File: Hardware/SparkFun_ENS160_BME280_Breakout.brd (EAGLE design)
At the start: 25.4 x 25.4 mm, 65 parts, among them J1 Qwiic Right Angle, J3 Qwiic Right Angle, J4 PTH, U1 AP2127K-1.8V, U2 ENS-160, U3 BME280

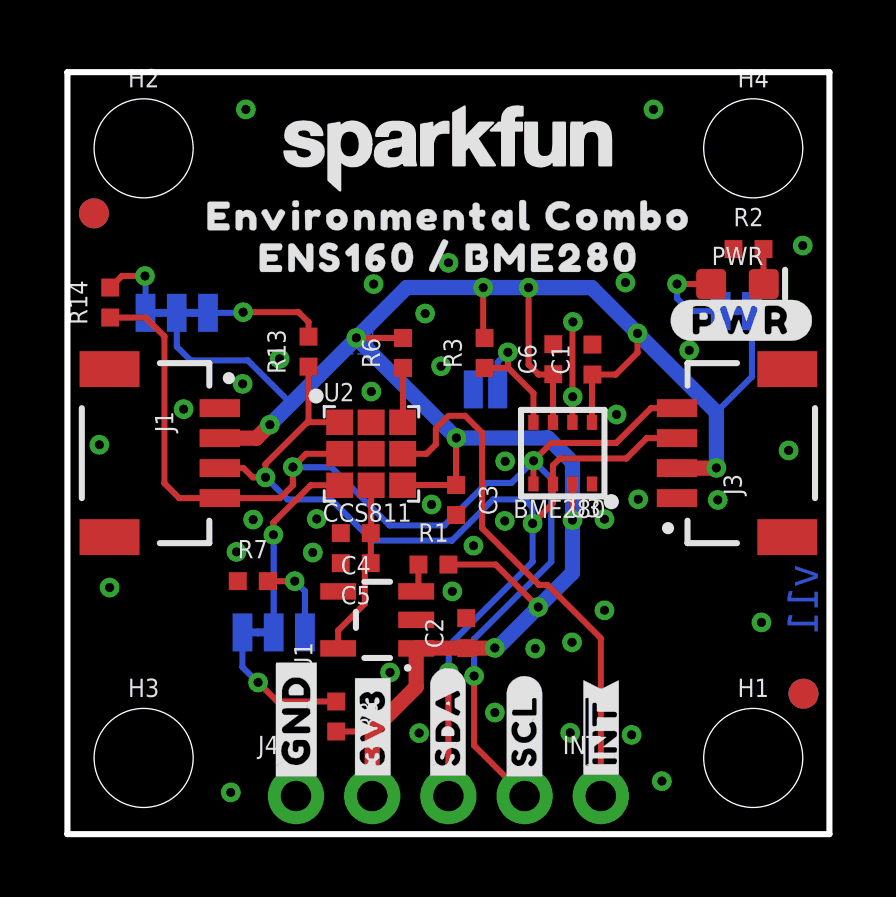
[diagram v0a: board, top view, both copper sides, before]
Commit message: group review changes - qwiic logos, via nudging
-added Qwiic logos to top silk
-nudged some filter caps near the ENS160 to allow even better GND flow
-removed old "ADDR" silk object on bottom silk.
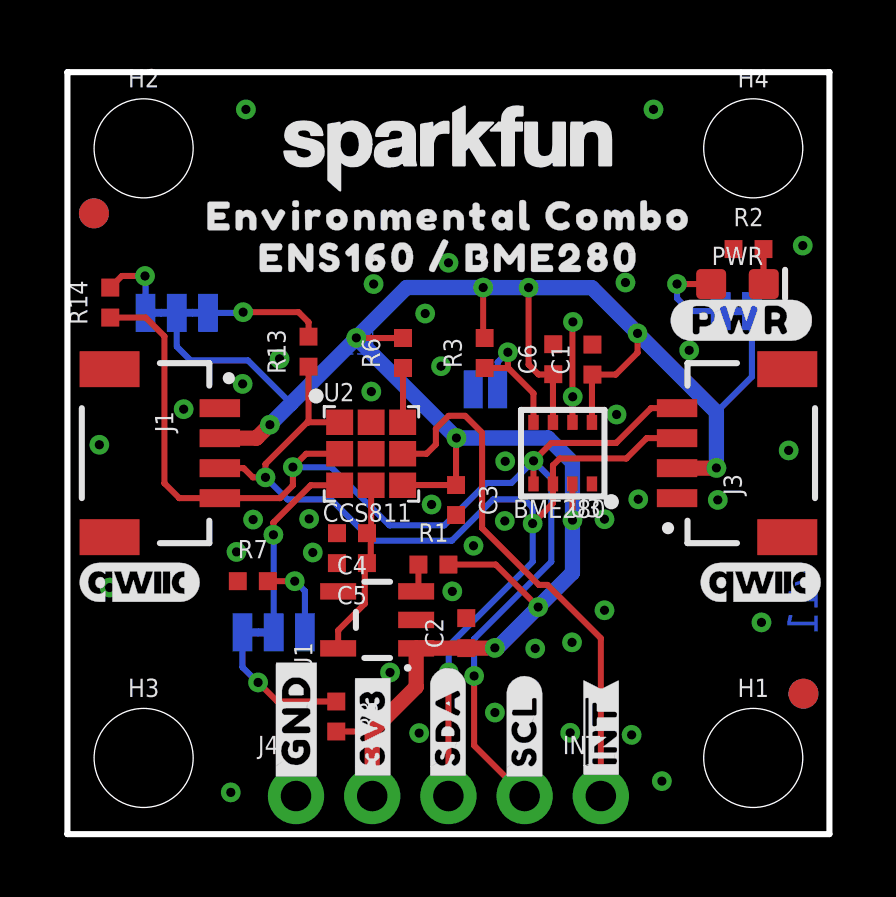
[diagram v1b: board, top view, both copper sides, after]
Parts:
- added U$20, U$21: (no value), SparkFun-Aesthetics:QWIIC_4MM
- moved U$17 0.38 mm to (17.9, 11.7)
- moved U$16 0.13 mm to (17.0, 13.1)
- moved C4 0.13 mm to (9.49, 10.0)
- moved C5 0.13 mm to (9.48, 9.03)
- moved U$61 0.13 mm to (9.84, 13.1)
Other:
- board text removed: "ADR1"
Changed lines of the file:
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@@
 <setting verticaltext="up"/>
 </settings>
-<grid distance="0.05" unitdist="inch" unit="inch" style="lines" multiple="1" display="yes" altdistance="0.0001" altunitdist="inch" altunit="inch"/>
+<grid distance="0.05" unitdist="inch" unit="inch" style="lines" multiple="1" display="yes" altdistance="0.005" altunitdist="inch" altunit="inch"/>
 <layers>
 <layer number="1" name="Top" color="4" fill="1" visible="yes" active="yes"/>
@@
 <wire x1="25.4" y1="0" x2="0" y2="0" width="0.2032" layer="20"/>
 <text x="24.50591875" y="7.8105" size="1.016" layer="16" ratio="20" rot="SMR270" align="center">v11</text>
-<text x="4.572" y="12.827" size="0.889" layer="22" font="vector" ratio="15" rot="MR90" align="center">ADR1</text>
 <text x="16.51" y="-21.59" size="1.778" layer="51">Nathan Seidle</text>
 <text x="8.509" y="10.414" size="0.6096" layer="25">CCS811</text>
@@
 1oz copper
 Finish: HASL</text>
-<wire x1="12.227565625" y1="13.749015625" x2="12.278359375" y2="12.748259375" width="0.1524" layer="22" curve="-126.475581"/>
-<wire x1="7.442196875" y1="12.763503125" x2="7.4701375" y2="13.73631875" width="0.1524" layer="22" curve="-126.475581"/>
+<wire x1="12.227565625" y1="13.622015625" x2="12.278359375" y2="12.621259375" width="0.1524" layer="22" curve="-126.475581"/>
+<wire x1="7.442196875" y1="12.636503125" x2="7.4701375" y2="13.60931875" width="0.1524" layer="22" curve="-126.475581"/>
 <dimension x1="25.4" y1="0" x2="22.33421875" y2="18.336259375" x3="29.8958" y3="9.168128125" textsize="1.778" layer="47" dtype="vertical" unit="inch"/>
 <dimension x1="0" y1="0" x2="5.08" y2="12.7" x3="-6.35" y3="6.35" textsize="1.778" layer="47" dtype="vertical" unit="inch"/>
@@
 <attribute name="VALUE" x="12.192" y="11.137" size="0.6096" layer="27" font="vector" ratio="20" rot="R270" align="top-center"/>
 </element>
-<element name="C4" library="SparkFun-Capacitors" package="0402-TIGHT" value="10uF" x="9.613" y="10.033" smashed="yes" rot="R180">
-<attribute name="NAME" x="9.613" y="9.271" size="0.6096" layer="25" font="vector" ratio="20" rot="R180" align="bottom-center"/>
-<attribute name="PROD_ID" value="CAP-14848" x="17.233" y="8.763" size="1.778" layer="27" font="vector" ratio="15" rot="R180" display="off"/>
-<attribute name="VALUE" x="9.613" y="10.795" size="0.6096" layer="27" font="vector" ratio="20" rot="R180" align="top-center"/>
+<element name="C4" library="SparkFun-Capacitors" package="0402-TIGHT" value="10uF" x="9.486" y="10.033" smashed="yes" rot="R180">
+<attribute name="NAME" x="9.486" y="9.271" size="0.6096" layer="25" font="vector" ratio="20" rot="R180" align="bottom-center"/>
+<attribute name="PROD_ID" value="CAP-14848" x="17.106" y="8.763" size="1.778" layer="27" font="vector" ratio="15" rot="R180" display="off"/>
+<attribute name="VALUE" x="9.486" y="10.795" size="0.6096" layer="27" font="vector" ratio="20" rot="R180" align="top-center"/>
 </element>
 <element name="ENS_ADR" library="SparkFun-Jumpers" package="SMT-JUMPER_3_1-NC_TRACE_SILK" package3d_urn="urn:adsk.eagle:package:39288/1" value="JUMPER-SMT_3_1-NC_TRACE_SILK" x="6.875778125" y="6.72591875" smashed="yes" rot="MR0">
@@
 <attribute name="VALUE" x="14.056359375" y="6.70141875" size="0.6096" layer="27" font="vector" ratio="20" rot="R90" align="top-center"/>
 </element>
-<element name="C5" library="SparkFun-Capacitors" package="0402-TIGHT" value="1.0uF" x="9.610459375" y="9.03478125" smashed="yes" rot="R180">
-<attribute name="NAME" x="9.610459375" y="8.27278125" size="0.6096" layer="25" font="vector" ratio="20" rot="R180" align="bottom-center"/>
-<attribute name="PROD_ID" value="CAP-12417" x="17.230459375" y="6.49478125" size="1.778" layer="27" font="vector" ratio="15" rot="R180" display="off"/>
-<attribute name="VALUE" x="9.610459375" y="9.79678125" size="0.6096" layer="27" font="vector" ratio="20" rot="R180" align="top-center"/>
+<element name="C5" library="SparkFun-Capacitors" package="0402-TIGHT" value="1.0uF" x="9.483459375" y="9.03478125" smashed="yes" rot="R180">
+<attribute name="NAME" x="9.483459375" y="8.27278125" size="0.6096" layer="25" font="vector" ratio="20" rot="R180" align="bottom-center"/>
+<attribute name="PROD_ID" value="CAP-12417" x="17.103459375" y="6.49478125" size="1.778" layer="27" font="vector" ratio="15" rot="R180" display="off"/>
+<attribute name="VALUE" x="9.483459375" y="9.79678125" size="0.6096" layer="27" font="vector" ratio="20" rot="R180" align="top-center"/>
 </element>
 <element name="R1" library="SparkFun-Resistors" package="0402-TIGHT" value="10k" x="12.19961875" y="8.98651875" smashed="yes">
@@
 <element name="U$11" library="output" package="ENVIRONMENTAL_COMBO0" value="" x="12.633959375" y="20.622259375" smashed="yes" rot="MR0"/>
 <element name="U$12" library="output" package="ENS160_#_BME2800" value="" x="12.628878125" y="19.232878125" smashed="yes" rot="MR0"/>
-<element name="U$16" library="output" package="OPEN#0X770" value="" x="16.9697375" y="13.208" smashed="yes" rot="MR0"/>
-<element name="U$17" library="output" package="CLOSED#0X760" value="" x="17.912078125" y="12.049759375" smashed="yes" rot="MR0"/>
+<element name="U$16" library="output" package="OPEN#0X770" value="" x="16.9697375" y="13.081" smashed="yes" rot="MR0"/>
+<element name="U$17" library="output" package="CLOSED#0X760" value="" x="17.912078125" y="11.668759375" smashed="yes" rot="MR0"/>
 <element name="U$1" library="output" package="#BME_ADR#0" value="" x="18.73758125" y="14.86408125" smashed="yes" rot="MR0"/>
 <element name="U$5" library="output" package="#ENS_ADR#0" value="" x="6.77418125" y="8.333740625" smashed="yes" rot="MR0"/>
-<element name="U$61" library="output" package="DEFAULT0" value="" x="9.842503125" y="13.27658125" smashed="yes" rot="MR0"/>
+<element name="U$61" library="output" package="DEFAULT0" value="" x="9.842503125" y="13.14958125" smashed="yes" rot="MR0"/>
 <element name="U$13" library="output" package="DEFAULT0" value="" x="2.9184625" y="5.3695625" smashed="yes" rot="MR0"/>
 <element name="U$15" library="output" package="#PWR#0" value="" x="22.463759375" y="17.12721875" smashed="yes"/>
@@
 <attribute name="VALUE" x="16.7570375" y="15.831821875" size="0.6096" layer="27" font="vector" ratio="20" rot="R90" align="top-center"/>
 </element>
+<element name="U$20" library="SparkFun-Aesthetics" package="QWIIC_4MM" value="" x="23.114" y="8.382" smashed="yes"/>
+<element name="U$21" library="SparkFun-Aesthetics" package="QWIIC_4MM" value="" x="2.413" y="8.382" smashed="yes"/>
 </elements>
 <signals>
@@
 <via x="20.726403125" y="16.129003125" extent="1-16" drill="0.3048"/>
 <via x="18.305784375" y="13.987784375" extent="1-16" drill="0.3048"/>
-<via x="8.310884375" y="10.50798125" extent="1-16" drill="0.3048"/>
+<via x="8.056884375" y="10.50798125" extent="1-16" drill="0.3048"/>
 <via x="12.1386625" y="10.988040625" extent="1-16" drill="0.3048"/>
 <via x="17.901921875" y="7.462521875" extent="1-16" drill="0.3048"/>
@@
 <contactref element="U1" pad="5"/>
 <contactref element="C5" pad="1"/>
-<wire x1="9.912340625" y1="8.8366625" x2="10.110459375" y2="9.03478125" width="0.2032" layer="1"/>
-<wire x1="9.912340625" y1="8.8366625" x2="9.912340625" y2="7.67968125" width="0.2032" layer="1"/>
+<wire x1="9.912340625" y1="8.9636625" x2="9.983459375" y2="9.03478125" width="0.2032" layer="1"/>
+<wire x1="9.912340625" y1="8.9636625" x2="9.912340625" y2="7.67968125" width="0.2032" layer="1"/>
 <wire x1="9.912340625" y1="7.67968125" x2="9.025" y2="6.792340625" width="0.2032" layer="1"/>
 <wire x1="9.025" y1="6.192478125" x2="9.025" y2="6.792340625" width="0.2032" layer="1"/>
-<wire x1="10.110459375" y1="9.03478125" x2="10.113" y2="9.037321875" width="0.2032" layer="1"/>
-<wire x1="10.113" y1="9.037321875" x2="10.113" y2="10.033" width="0.2032" layer="1"/>
-<wire x1="10.113" y1="10.033" x2="10.125" y2="10.045" width="0.2032" layer="1"/>
-<wire x1="10.125" y1="10.045" x2="10.125" y2="11.63" width="0.2032" layer="1"/>
+<wire x1="9.983459375" y1="9.03478125" x2="10.113" y2="9.164321875" width="0.2032" layer="1"/>
+<wire x1="10.113" y1="9.906" x2="9.986" y2="10.033" width="0.2032" layer="1"/>
+<wire x1="10.113" y1="9.906" x2="10.113" y2="9.164321875" width="0.2032" layer="1"/>
+<wire x1="9.986" y1="10.033" x2="10.125" y2="10.172" width="0.2032" layer="1"/>
+<wire x1="10.125" y1="10.172" x2="10.125" y2="11.63" width="0.2032" layer="1"/>
 </signal>
 <signal name="ADDR">

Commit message: checklist run eng
-VCC ranges added for bME280
-corrected BME_ADR jumper comment
-moved ENS160 to SFE library
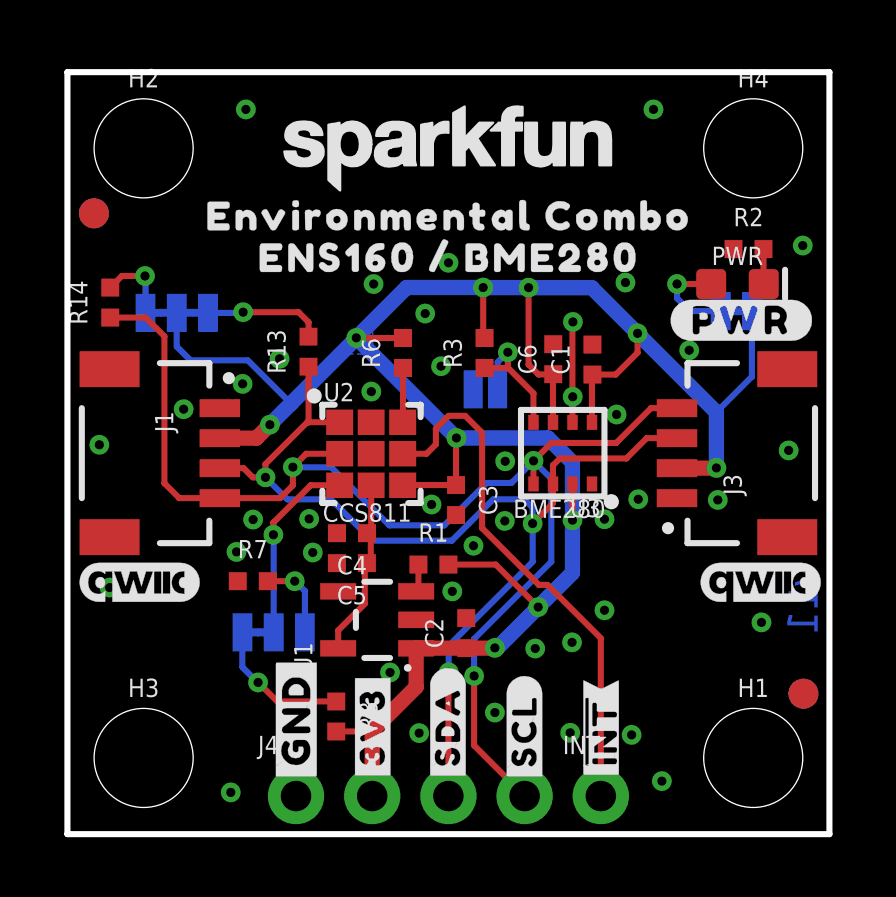
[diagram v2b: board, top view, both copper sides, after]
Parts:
- U2: value ENS-160 -> ENS160
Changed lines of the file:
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@@
 <element name="LOGO3" library="SparkFun-Aesthetics" package="SFE_LOGO_NAME_.1@1" value="SFE_LOGO_NAME.1_INCH" x="18.669" y="20.93595" smashed="yes" rot="MR0"/>
 <element name="U$59" library="SparkFun-Aesthetics" package="ORDERING_INSTRUCTIONS" value="" x="44.45" y="50.8" smashed="yes"/>
-<element name="U2" library="SparkFun-Sensors" package="LGA-9" value="ENS-160" x="10.16" y="12.7" smashed="yes">
+<element name="U2" library="SparkFun-Sensors" package="LGA-9" value="ENS160" x="10.16" y="12.7" smashed="yes">
 <attribute name="NAME" x="8.5344" y="14.4272" size="0.6096" layer="25" font="vector" ratio="20"/>
 <attribute name="PROD_ID" value="IC-17100" x="5.08" y="19.05" size="1.778" layer="27" font="vector" ratio="15" display="off"/>
-<attribute name="VALUE" x="8.4074" y="10.3124" size="0.6096" layer="27" font="vector" ratio="20"/>
+<attribute name="VALUE" value="ENS160" x="8.4074" y="10.3124" size="0.6096" layer="27" font="vector" ratio="20"/>
 </element>
 <element name="R6" library="SparkFun-Resistors" package="0402-TIGHT" value="10k" x="11.186159375" y="16.037559375" smashed="yes" rot="R90">
